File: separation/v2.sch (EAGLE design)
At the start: 6 parts

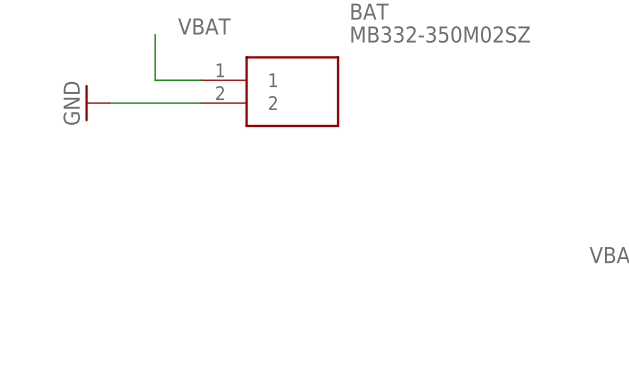
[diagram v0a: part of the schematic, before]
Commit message: add potential divider
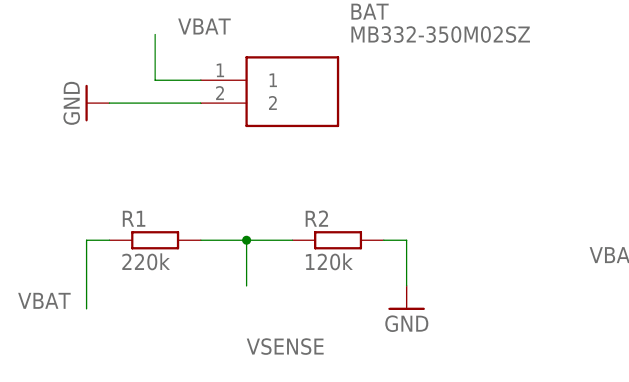
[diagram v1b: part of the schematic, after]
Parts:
- added R1: 220k, rcl:R-EU_0204/7
- added R2: 120k, rcl:R-EU_0204/7
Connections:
- new net VSENSE: R1.2, R2.1
- net GND: now also R2.2
- net VBAT: now also R1.1
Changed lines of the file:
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@@
 <part name="GND4" library="supply1" library_urn="urn:adsk.eagle:library:371" deviceset="GND" device=""/>
 <part name="GND5" library="supply1" library_urn="urn:adsk.eagle:library:371" deviceset="GND" device=""/>
+<part name="R1" library="rcl" library_urn="urn:adsk.eagle:library:334" deviceset="R-EU_" device="0204/7" package3d_urn="urn:adsk.eagle:package:23498/2" value="220k"/>
+<part name="R2" library="rcl" library_urn="urn:adsk.eagle:library:334" deviceset="R-EU_" device="0204/7" package3d_urn="urn:adsk.eagle:package:23498/2" value="120k"/>
+<part name="GND6" library="supply1" library_urn="urn:adsk.eagle:library:371" deviceset="GND" device=""/>
 </parts>
 <sheets>
@@
 <attribute name="VALUE" x="104.14" y="33.02" size="1.778" layer="96" rot="MR90"/>
 </instance>
+<instance part="R1" gate="G$1" x="-20.32" y="-7.62" smashed="yes">
+<attribute name="NAME" x="-24.13" y="-6.1214" size="1.778" layer="95"/>
+<attribute name="VALUE" x="-24.13" y="-10.922" size="1.778" layer="96"/>
+</instance>
+<instance part="R2" gate="G$1" x="0" y="-7.62" smashed="yes">
+<attribute name="NAME" x="-3.81" y="-6.1214" size="1.778" layer="95"/>
+<attribute name="VALUE" x="-3.81" y="-10.922" size="1.778" layer="96"/>
+</instance>
+<instance part="GND6" gate="1" x="7.62" y="-15.24" smashed="yes" rot="MR0">
+<attribute name="VALUE" x="10.16" y="-17.78" size="1.778" layer="96" rot="MR0"/>
+</instance>
 </instances>
 <busses>
@@
 <wire x1="109.22" y1="35.56" x2="119.38" y2="35.56" width="0.1524" layer="91"/>
 </segment>
+<segment>
+<pinref part="R2" gate="G$1" pin="2"/>
+<pinref part="GND6" gate="1" pin="GND"/>
+<wire x1="5.08" y1="-7.62" x2="7.62" y2="-7.62" width="0.1524" layer="91"/>
+<wire x1="7.62" y1="-7.62" x2="7.62" y2="-12.7" width="0.1524" layer="91"/>
+</segment>
 </net>
 <net name="MOSI" class="0">
@@
 <label x="27.94" y="-10.16" size="1.778" layer="95"/>
 </segment>
+<segment>
+<pinref part="R1" gate="G$1" pin="1"/>
+<wire x1="-25.4" y1="-7.62" x2="-27.94" y2="-7.62" width="0.1524" layer="91"/>
+<wire x1="-27.94" y1="-7.62" x2="-27.94" y2="-15.24" width="0.1524" layer="91"/>
+<label x="-35.56" y="-15.24" size="1.778" layer="95"/>
+</segment>
 </net>
 <net name="SERVO" class="0">
@@
 <wire x1="114.3" y1="38.1" x2="114.3" y2="45.72" width="0.1524" layer="91"/>
 <label x="116.84" y="45.72" size="1.778" layer="95"/>
+</segment>
+</net>
+<net name="VSENSE" class="0">
+<segment>
+<pinref part="R1" gate="G$1" pin="2"/>
+<pinref part="R2" gate="G$1" pin="1"/>
+<wire x1="-15.24" y1="-7.62" x2="-10.16" y2="-7.62" width="0.1524" layer="91"/>
+<wire x1="-10.16" y1="-7.62" x2="-5.08" y2="-7.62" width="0.1524" layer="91"/>
+<wire x1="-10.16" y1="-7.62" x2="-10.16" y2="-12.7" width="0.1524" layer="91"/>
+<junction x="-10.16" y="-7.62"/>
+<label x="-10.16" y="-20.32" size="1.778" layer="95"/>
 </segment>
 </net>
@@
 packages will not be understood (or retained) with this version.
 </note>
+<note version="8.4" severity="warning">
+Since Version 8.4, EAGLE supports properties for SPICE simulation.
+Probes in schematics and SPICE mapping objects found in parts and library devices
+will not be understood with this version. Update EAGLE to the latest version
+for full support of SPICE simulation.
+</note>
 </compatibility>

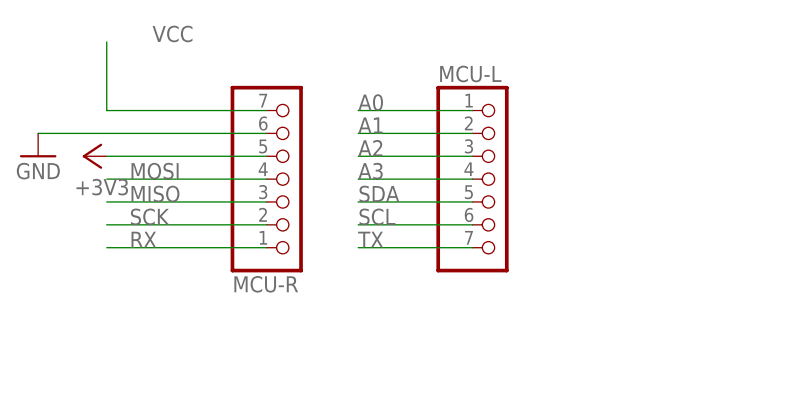
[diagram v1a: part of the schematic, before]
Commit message: connect comps to pins
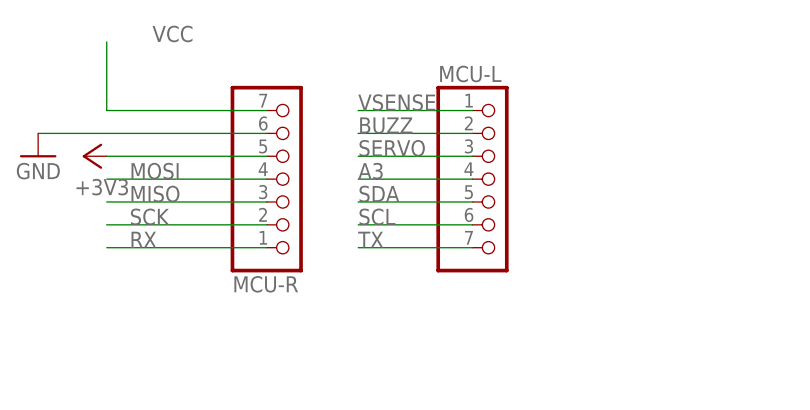
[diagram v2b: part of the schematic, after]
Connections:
- removed net A0: MCU-L.1
- removed net A1: MCU-L.2
- removed net A2: MCU-L.3
- net BUZZ: now also MCU-L.2
- net SERVO: now also MCU-L.3
- net VSENSE: now also MCU-L.1
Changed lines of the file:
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@@
-</segment>
-</net>
-<net name="A2" class="0">
-<segment>
-<label x="45.72" y="60.96" size="1.778" layer="95"/>
-<pinref part="MCU-L" gate="A" pin="3"/>
-<wire x1="45.72" y1="60.96" x2="58.42" y2="60.96" width="0.1524" layer="91"/>
-</segment>
-</net>
-<net name="A1" class="0">
-<segment>
-<pinref part="MCU-L" gate="A" pin="2"/>
-<wire x1="58.42" y1="63.5" x2="45.72" y2="63.5" width="0.1524" layer="91"/>
-<label x="45.72" y="63.5" size="1.778" layer="95"/>
 </segment>
 </net>
@@
 <pinref part="MCU-R" gate="A" pin="5"/>
 <pinref part="+3V1" gate="G$1" pin="+3V3"/>
-</segment>
-</net>
-<net name="A0" class="0">
-<segment>
-<label x="45.72" y="66.04" size="1.778" layer="95"/>
-<pinref part="MCU-L" gate="A" pin="1"/>
-<wire x1="45.72" y1="66.04" x2="58.42" y2="66.04" width="0.1524" layer="91"/>
 </segment>
 </net>
@@
 <label x="-27.94" y="30.48" size="1.778" layer="95"/>
 </segment>
+<segment>
+<label x="45.72" y="60.96" size="1.778" layer="95"/>
+<pinref part="MCU-L" gate="A" pin="3"/>
+<wire x1="45.72" y1="60.96" x2="58.42" y2="60.96" width="0.1524" layer="91"/>
+</segment>
 </net>
 <net name="BUZZ" class="0">
@@
 <wire x1="114.3" y1="38.1" x2="114.3" y2="45.72" width="0.1524" layer="91"/>
 <label x="116.84" y="45.72" size="1.778" layer="95"/>
+</segment>
+<segment>
+<pinref part="MCU-L" gate="A" pin="2"/>
+<wire x1="58.42" y1="63.5" x2="45.72" y2="63.5" width="0.1524" layer="91"/>
+<label x="45.72" y="63.5" size="1.778" layer="95"/>
 </segment>
 </net>
@@
 <label x="-10.16" y="-20.32" size="1.778" layer="95"/>
 </segment>
+<segment>
+<label x="45.72" y="66.04" size="1.778" layer="95"/>
+<pinref part="MCU-L" gate="A" pin="1"/>
+<wire x1="45.72" y1="66.04" x2="58.42" y2="66.04" width="0.1524" layer="91"/>
+</segment>
 </net>

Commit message: replace resistor footprint with smaller version
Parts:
- R1, R2: device rcl:R-EU_0204/7 -> rcl:R-EU_0204/2V
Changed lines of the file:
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@@
 <part name="GND4" library="supply1" library_urn="urn:adsk.eagle:library:371" deviceset="GND" device=""/>
 <part name="GND5" library="supply1" library_urn="urn:adsk.eagle:library:371" deviceset="GND" device=""/>
-<part name="R1" library="rcl" library_urn="urn:adsk.eagle:library:334" deviceset="R-EU_" device="0204/7" package3d_urn="urn:adsk.eagle:package:23498/2" value="220k"/>
-<part name="R2" library="rcl" library_urn="urn:adsk.eagle:library:334" deviceset="R-EU_" device="0204/7" package3d_urn="urn:adsk.eagle:package:23498/2" value="120k"/>
+<part name="R1" library="rcl" library_urn="urn:adsk.eagle:library:334" deviceset="R-EU_" device="0204/2V" package3d_urn="urn:adsk.eagle:package:23495/1" value="220k"/>
+<part name="R2" library="rcl" library_urn="urn:adsk.eagle:library:334" deviceset="R-EU_" device="0204/2V" package3d_urn="urn:adsk.eagle:package:23495/1" value="120k"/>
 <part name="GND6" library="supply1" library_urn="urn:adsk.eagle:library:371" deviceset="GND" device=""/>
 </parts>

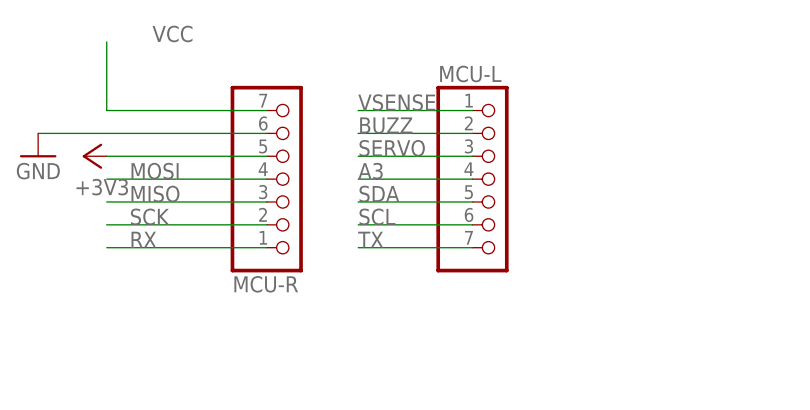
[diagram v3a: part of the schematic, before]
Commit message: reorder IO pins
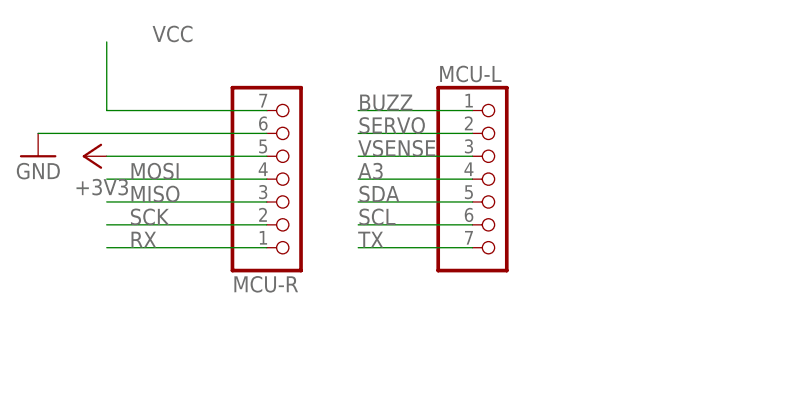
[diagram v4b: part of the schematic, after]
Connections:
- net BUZZ: now also MCU-L.1; no longer MCU-L.2
- net SERVO: now also MCU-L.2; no longer MCU-L.3
- net VSENSE: now also MCU-L.3; no longer MCU-L.1
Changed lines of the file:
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@@
 </segment>
 <segment>
-<label x="45.72" y="60.96" size="1.778" layer="95"/>
-<pinref part="MCU-L" gate="A" pin="3"/>
-<wire x1="45.72" y1="60.96" x2="58.42" y2="60.96" width="0.1524" layer="91"/>
+<pinref part="MCU-L" gate="A" pin="2"/>
+<wire x1="58.42" y1="63.5" x2="45.72" y2="63.5" width="0.1524" layer="91"/>
+<label x="45.72" y="63.5" size="1.778" layer="95"/>
 </segment>
 </net>
@@
 </segment>
 <segment>
-<pinref part="MCU-L" gate="A" pin="2"/>
-<wire x1="58.42" y1="63.5" x2="45.72" y2="63.5" width="0.1524" layer="91"/>
-<label x="45.72" y="63.5" size="1.778" layer="95"/>
+<label x="45.72" y="66.04" size="1.778" layer="95"/>
+<pinref part="MCU-L" gate="A" pin="1"/>
+<wire x1="45.72" y1="66.04" x2="58.42" y2="66.04" width="0.1524" layer="91"/>
 </segment>
 </net>
@@
 </segment>
 <segment>
-<label x="45.72" y="66.04" size="1.778" layer="95"/>
-<pinref part="MCU-L" gate="A" pin="1"/>
-<wire x1="45.72" y1="66.04" x2="58.42" y2="66.04" width="0.1524" layer="91"/>
+<label x="45.72" y="60.96" size="1.778" layer="95"/>
+<pinref part="MCU-L" gate="A" pin="3"/>
+<wire x1="45.72" y1="60.96" x2="58.42" y2="60.96" width="0.1524" layer="91"/>
 </segment>
 </net>

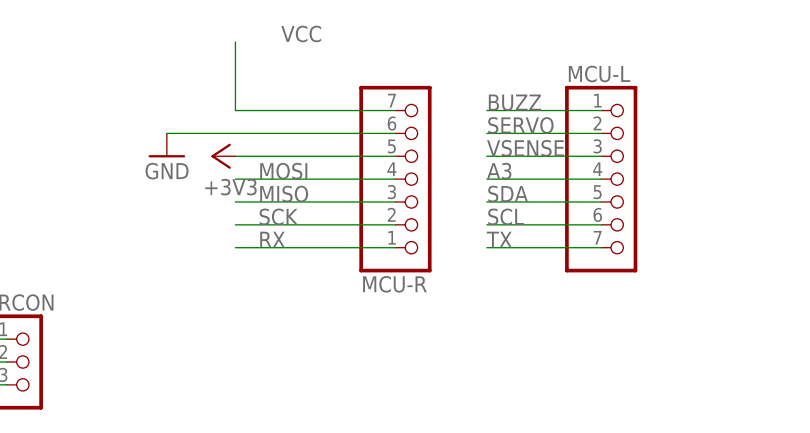
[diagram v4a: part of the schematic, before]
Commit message: move buzzer PWM out to MISO pin
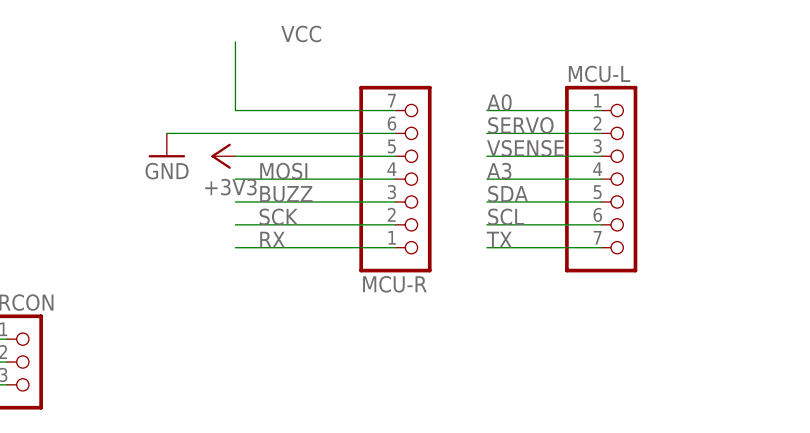
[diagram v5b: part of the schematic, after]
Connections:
- removed net MISO: MCU-R.3
- new net A0: MCU-L.1
- net BUZZ: now also MCU-R.3; no longer MCU-L.1
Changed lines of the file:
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@@
-</segment>
-</net>
-<net name="MISO" class="0">
-<segment>
-<wire x1="35.56" y1="55.88" x2="17.78" y2="55.88" width="0.1524" layer="91"/>
-<label x="20.32" y="55.88" size="1.778" layer="95"/>
-<pinref part="MCU-R" gate="A" pin="3"/>
 </segment>
 </net>
@@
 </segment>
 <segment>
-<label x="45.72" y="66.04" size="1.778" layer="95"/>
-<pinref part="MCU-L" gate="A" pin="1"/>
-<wire x1="45.72" y1="66.04" x2="58.42" y2="66.04" width="0.1524" layer="91"/>
+<wire x1="35.56" y1="55.88" x2="17.78" y2="55.88" width="0.1524" layer="91"/>
+<label x="20.32" y="55.88" size="1.778" layer="95"/>
+<pinref part="MCU-R" gate="A" pin="3"/>
 </segment>
 </net>
@@
 </segment>
 </net>
+<net name="A0" class="0">
+<segment>
+<label x="45.72" y="66.04" size="1.778" layer="95"/>
+<pinref part="MCU-L" gate="A" pin="1"/>
+<wire x1="45.72" y1="66.04" x2="58.42" y2="66.04" width="0.1524" layer="91"/>
+</segment>
+</net>

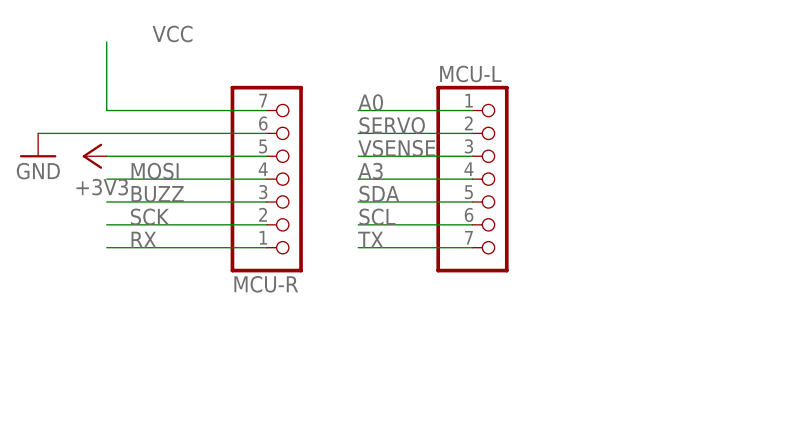
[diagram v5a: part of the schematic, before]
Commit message: swap vsense and servo pins on mcu
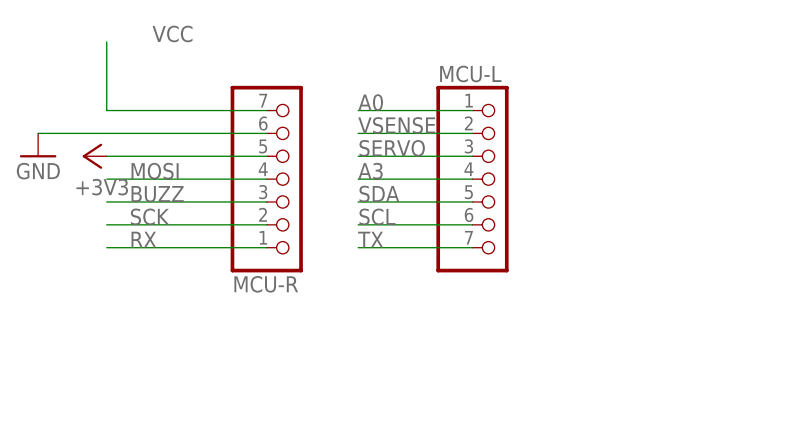
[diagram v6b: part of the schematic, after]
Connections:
- net SERVO: now also MCU-L.3; no longer MCU-L.2
- net VSENSE: now also MCU-L.2; no longer MCU-L.3
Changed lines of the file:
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@@
 </segment>
 <segment>
-<pinref part="MCU-L" gate="A" pin="2"/>
-<wire x1="58.42" y1="63.5" x2="45.72" y2="63.5" width="0.1524" layer="91"/>
-<label x="45.72" y="63.5" size="1.778" layer="95"/>
+<label x="45.72" y="60.96" size="1.778" layer="95"/>
+<pinref part="MCU-L" gate="A" pin="3"/>
+<wire x1="45.72" y1="60.96" x2="58.42" y2="60.96" width="0.1524" layer="91"/>
 </segment>
 </net>
@@
 </segment>
 <segment>
-<label x="45.72" y="60.96" size="1.778" layer="95"/>
-<pinref part="MCU-L" gate="A" pin="3"/>
-<wire x1="45.72" y1="60.96" x2="58.42" y2="60.96" width="0.1524" layer="91"/>
+<pinref part="MCU-L" gate="A" pin="2"/>
+<wire x1="58.42" y1="63.5" x2="45.72" y2="63.5" width="0.1524" layer="91"/>
+<label x="45.72" y="63.5" size="1.778" layer="95"/>
 </segment>
 </net>

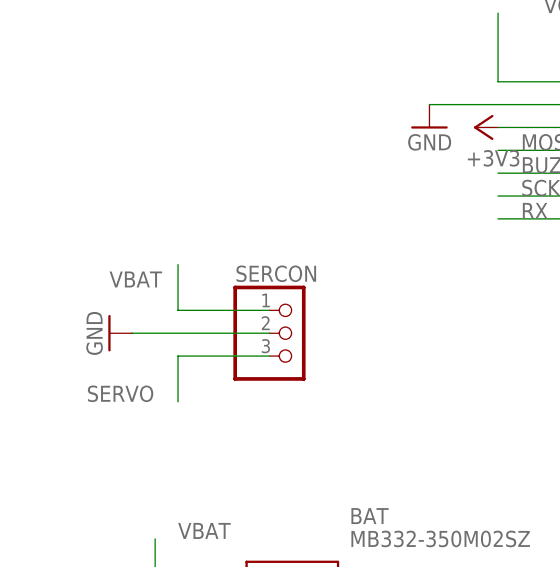
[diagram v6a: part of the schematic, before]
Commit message: change servo connector pinout to match flight servo
MG2611WHV
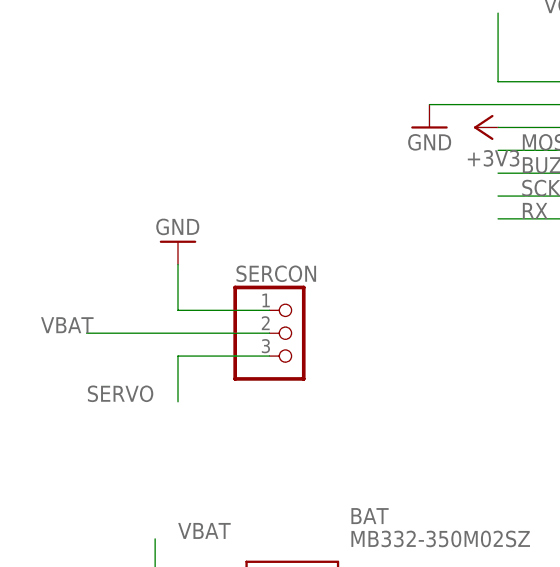
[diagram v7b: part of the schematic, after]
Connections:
- net GND: now also SERCON.1; no longer SERCON.2
- net VBAT: now also SERCON.2; no longer SERCON.1
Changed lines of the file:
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@@
 <attribute name="VALUE" x="-11.43" y="30.48" size="1.778" layer="96"/>
 </instance>
-<instance part="GND2" gate="1" x="-25.4" y="38.1" smashed="yes" rot="MR90">
-<attribute name="VALUE" x="-27.94" y="35.56" size="1.778" layer="96" rot="MR90"/>
+<instance part="GND2" gate="1" x="-17.78" y="48.26" smashed="yes" rot="MR180">
+<attribute name="VALUE" x="-20.32" y="50.8" size="1.778" layer="96" rot="MR180"/>
 </instance>
 <instance part="GND3" gate="1" x="-27.94" y="7.62" smashed="yes" rot="MR90">
@@
 </segment>
 <segment>
-<pinref part="SERCON" gate="A" pin="2"/>
-<wire x1="-7.62" y1="38.1" x2="-22.86" y2="38.1" width="0.1524" layer="91"/>
-<pinref part="GND2" gate="1" pin="GND"/>
-</segment>
-<segment>
 <pinref part="GND3" gate="1" pin="GND"/>
 <pinref part="BAT" gate="G$1" pin="2"/>
@@
 <wire x1="5.08" y1="-7.62" x2="7.62" y2="-7.62" width="0.1524" layer="91"/>
 <wire x1="7.62" y1="-7.62" x2="7.62" y2="-12.7" width="0.1524" layer="91"/>
+</segment>
+<segment>
+<pinref part="SERCON" gate="A" pin="1"/>
+<wire x1="-7.62" y1="40.64" x2="-17.78" y2="40.64" width="0.1524" layer="91"/>
+<pinref part="GND2" gate="1" pin="GND"/>
+<wire x1="-17.78" y1="40.64" x2="-17.78" y2="45.72" width="0.1524" layer="91"/>
 </segment>
 </net>
@@
 <net name="VBAT" class="0">
 <segment>
-<pinref part="SERCON" gate="A" pin="1"/>
-<wire x1="-7.62" y1="40.64" x2="-17.78" y2="40.64" width="0.1524" layer="91"/>
-<wire x1="-17.78" y1="40.64" x2="-17.78" y2="45.72" width="0.1524" layer="91"/>
-<label x="-25.4" y="43.18" size="1.778" layer="95"/>
-</segment>
-<segment>
 <pinref part="BAT" gate="G$1" pin="1"/>
 <wire x1="-15.24" y1="10.16" x2="-20.32" y2="10.16" width="0.1524" layer="91"/>
@@
 <label x="-35.56" y="-15.24" size="1.778" layer="95"/>
 </segment>
+<segment>
+<pinref part="SERCON" gate="A" pin="2"/>
+<wire x1="-7.62" y1="38.1" x2="-27.94" y2="38.1" width="0.1524" layer="91"/>
+<label x="-33.02" y="38.1" size="1.778" layer="95"/>
+</segment>
 </net>
